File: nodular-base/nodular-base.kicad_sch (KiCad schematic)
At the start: 0 parts

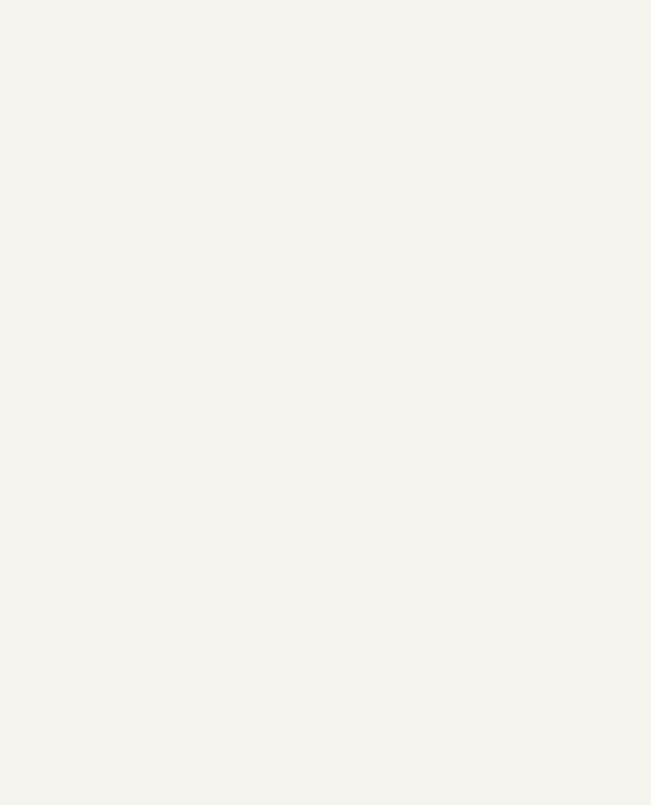
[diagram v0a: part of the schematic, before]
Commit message: Update layout for top board, add library items
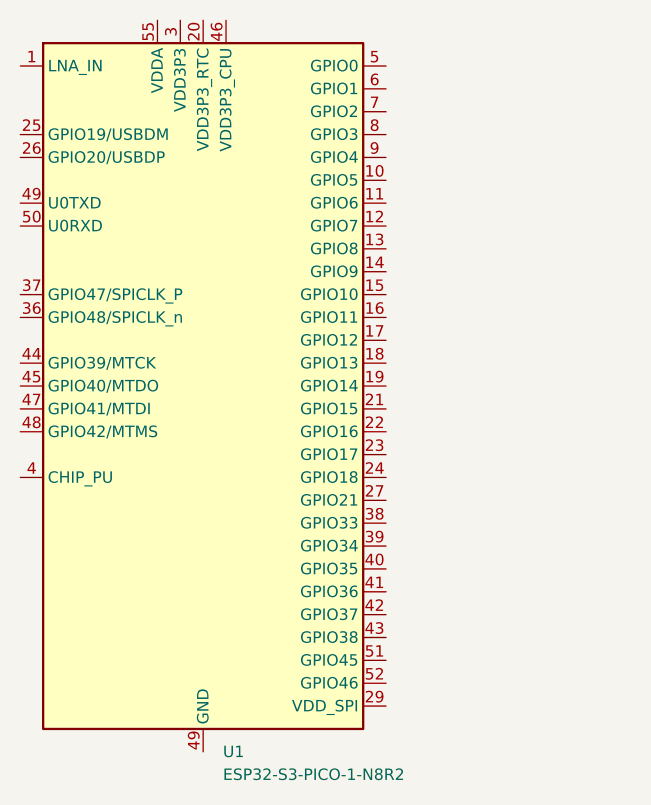
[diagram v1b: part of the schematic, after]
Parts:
- added U1: ESP32-S3-PICO-1-N8R2, Package_DFN_QFN:QFN-56-1EP_7x7mm_P0.4mm_EP4x4mm, symbol nodular:ESP32-S3-PICO-1-N8R2
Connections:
- new net: U1.2 (VDD3P3), U1.3 (VDD3P3)
- new net: U1.55 (VDDA), U1.56 (VDDA)
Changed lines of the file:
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@@
 (kicad_sch (version 20230121) (generator eeschema)
   (paper "A4")
+  (symbol (lib_id "nodular:ESP32-S3-PICO-1-N8R2") (at 90.17 100.33 0) (unit 1)
+    (in_bom yes) (on_board yes) (dnp no) (fields_autoplaced)
+    (property "Reference" "U1" (at 92.3641 140.97 0)
+      (effects (font (size 1.27 1.27)) (justify left))
+    )
+    (property "Value" "ESP32-S3-PICO-1-N8R2" (at 92.3641 143.51 0)
+      (effects (font (size 1.27 1.27)) (justify left))
+    )
+    (property "Footprint" "Package_DFN_QFN:QFN-56-1EP_7x7mm_P0.4mm_EP4x4mm" (at 90.17 143.51 0)
+      (effects (font (size 1.27 1.27)) hide)
+    )
+    (property "Datasheet" "" (at 90.17 145.796 0)
+      (effects (font (size 1.27 1.27)) hide)
+    )
+    (pin "36")
+    (pin "51")
+    (pin "44")
+    (pin "24")
+    (pin "21")
+    (pin "43")
+    (pin "35")
+    (pin "7")
+    (pin "22")
+    (pin "23")
+    (pin "16")
+    (pin "42")
+    (pin "9")
+    (pin "33")
+    (pin "2")
+    (pin "48")
+    (pin "50")
+    (pin "26")
+    (pin "34")
+    (pin "41")
+    (pin "37")
+    (pin "8")
+    (pin "46")
+    (pin "19")
+    (pin "49")
+    (pin "12")
+    (pin "13")
+    (pin "38")
+    (pin "52")
+    (pin "1")
+    (pin "11")
+    (pin "31")
+    (pin "14")
+    (pin "47")
+    (pin "15")
+    (pin "30")
+    (pin "18")
+    (pin "5")
+    (pin "10")
+    (pin "55")
+    (pin "45")
+    (pin "27")
+    (pin "56")
+    (pin "25")
+    (pin "32")
+    (pin "39")
+    (pin "6")
+    (pin "28")
+    (pin "29")
+    (pin "4")
+    (pin "3")
+    (pin "49")
+    (pin "17")
+    (pin "40")
+    (pin "20")
+    (instances
+      (project "nodular-base"
+        (path "/6dcb0502-87e2-4c28-9ce8-81aab8925f06"
+          (reference "U1") (unit 1)
+        )
+      )
+    )
+  )
   (sheet (at 180.34 64.77) (size 46.99 46.99) (fields_autoplaced)
     (stroke (width 0.1524) (type solid))

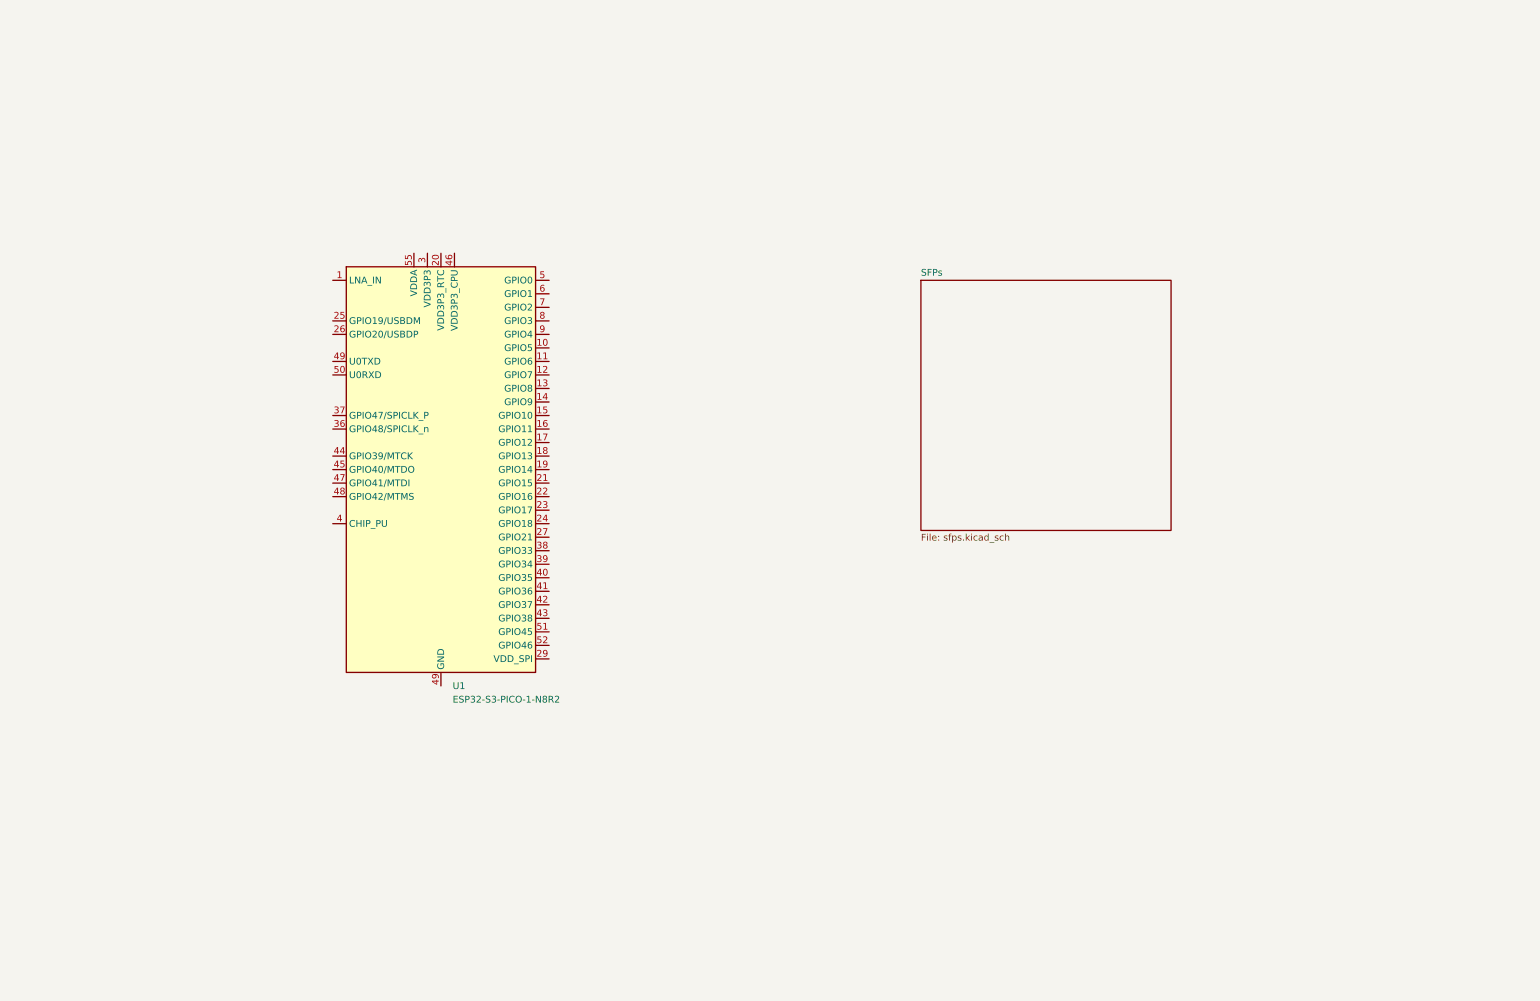
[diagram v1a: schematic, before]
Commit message: Nodular-base: Add most components onto baseboard for a test fit. Nodular-base: Add fps and models for solderable standoffs, replace solderable standoffs and reposition them. Nodule template: Adjust nodule template hole position, export STEP of nodule. Nodular-base: Add many components to schematic, structure schematic hierarchy Nodular-base: Route USB, RF path, and MCU decoupling
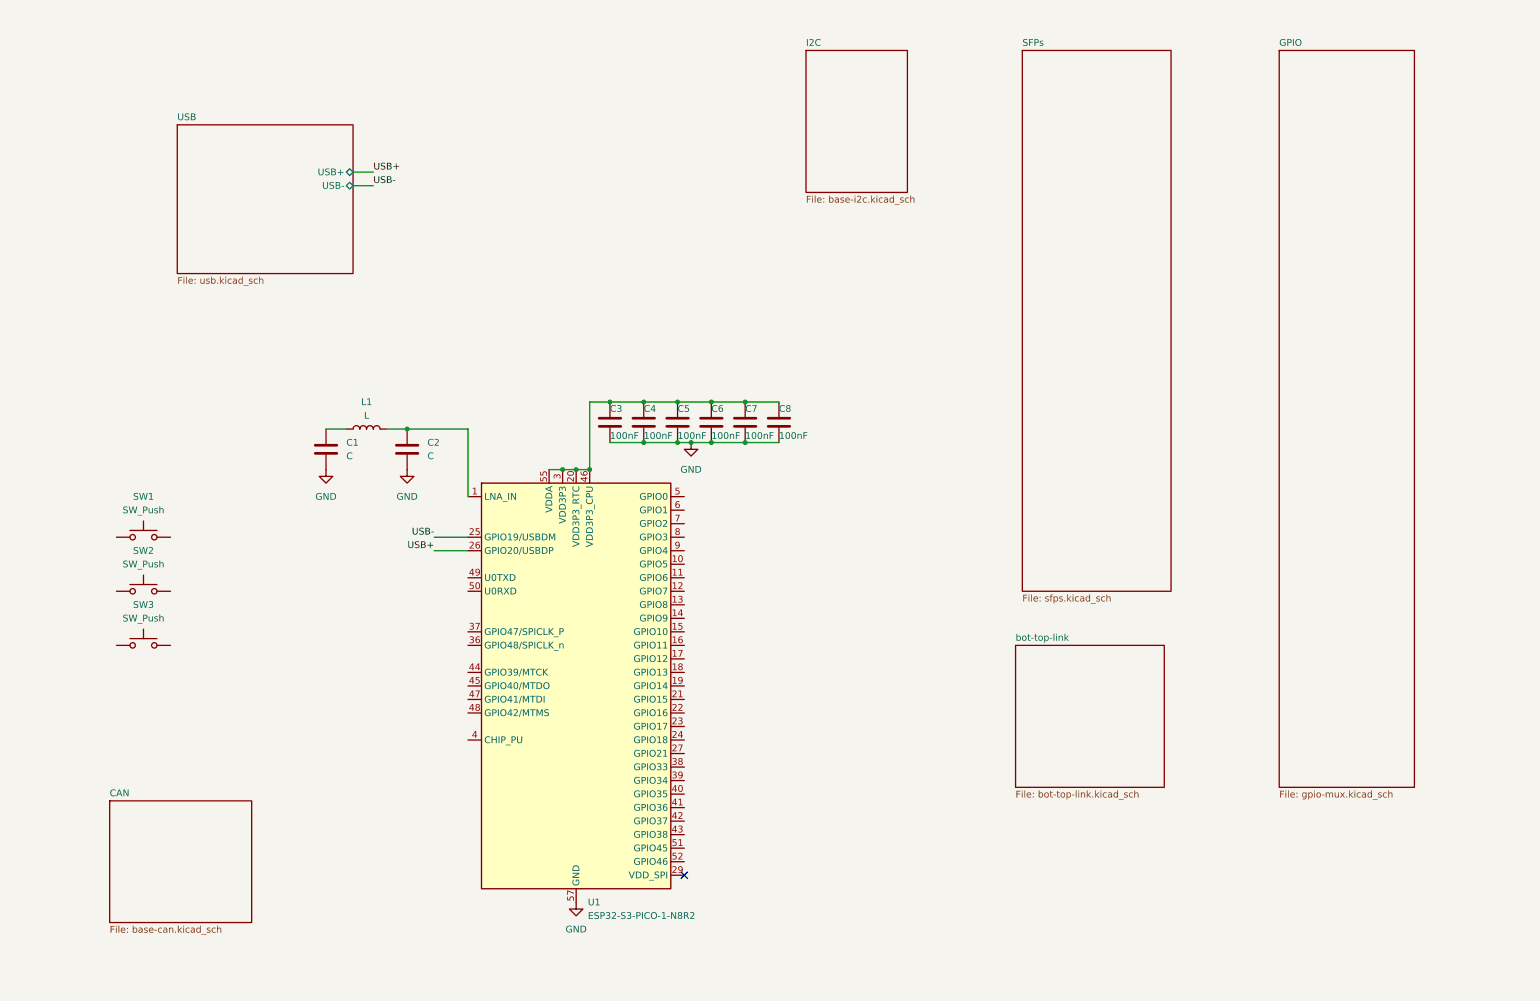
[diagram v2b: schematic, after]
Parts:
- added C1, C2: C, Capacitor_SMD:C_0402_1005Metric, symbol Device:C
- added C3, C4, C5, C6, C7, C8: 100nF, Capacitor_SMD:C_0402_1005Metric, symbol Device:C
- added L1: L, Inductor_SMD:L_0402_1005Metric, symbol Device:L
- added SW1, SW2, SW3: SW_Push, nodular:sidebutton-1TS003B-1400-3500A-CT, symbol Switch:SW_Push
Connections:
- net at U1.1 (LNA_IN): now also C2.1, L1.2
- net at U1.2 (VDD3P3), U1.3 (VDD3P3): now also U1.20 (VDD3P3_RTC), U1.46 (VDD3P3_CPU), U1.55 (VDDA), U1.56 (VDDA), C3.1, C4.1, C5.1, C6.1, C7.1, C8.1
- net USB-: now reaches U1.25 (GPIO19/USBDM)
- net USB+: now reaches U1.26 (GPIO20/USBDP)
- new net: C1.1, L1.1
- new net GND: C1.2, C2.2, C3.2, C4.2, C5.2, C6.2, C7.2, C8.2, U1.57 (GND)
- no-connect marks 0 -> 1
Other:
- added sheet CAN (base-can.kicad_sch)
- added sheet GPIO (gpio-mux.kicad_sch)
- added sheet I2C (base-i2c.kicad_sch)
- added sheet USB (usb.kicad_sch)
- added sheet bot-top-link (bot-top-link.kicad_sch)
- moved on the sheet: U1

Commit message: WIP layout for base
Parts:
- added C9: 22uF, Capacitor_SMD:C_1206_3216Metric, symbol Device:C
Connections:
- net GND: now also C9.2
- net 3V3_SYS: now reaches C3.1, C4.1, C5.1, C6.1, C7.1, C8.1, U1.2 (VDD3P3), U1.20 (VDD3P3_RTC), U1.3 (VDD3P3), U1.46 (VDD3P3_CPU), U1.55 (VDDA), U1.56 (VDDA)
- net 3V3_SYS: now also C9.1
- net NF_HS3: now reaches U1.10 (GPIO5)
- net NF_HS4: now reaches U1.11 (GPIO6)
- net ND_HS1: now reaches U1.16 (GPIO11)
- net ND_HS4: now reaches U1.17 (GPIO12)
- net ND_HS3: now reaches U1.18 (GPIO13)
- net ND_HS2: now reaches U1.19 (GPIO14)
- net NE_HS3: now reaches U1.21 (GPIO15)
- net NE_HS2: now reaches U1.22 (GPIO16)
- net NE_HS4: now reaches U1.23 (GPIO17)
- net NE_HS1: now reaches U1.24 (GPIO18)
- net LED_DATA: now reaches U1.27 (GPIO21)
- net NC_HS4: now reaches U1.36 (GPIO48/SPICLK_n)
- net NC_HS3: now reaches U1.37 (GPIO47/SPICLK_P)
- net NC_HS2: now reaches U1.38 (GPIO33)
- net NC_HS1: now reaches U1.39 (GPIO34)
- net NB_HS1: now reaches U1.40 (GPIO35)
- net NB_HS2: now reaches U1.41 (GPIO36)
- net NB_HS3: now reaches U1.42 (GPIO37)
- net NB_HS4: now reaches U1.43 (GPIO38)
- net NA_HS1: now reaches U1.44 (GPIO39/MTCK)
- net NA_HS2: now reaches U1.45 (GPIO40/MTDO)
- net NA_HS3: now reaches U1.47 (GPIO41/MTDI)
- net NA_HS4: now reaches U1.48 (GPIO42/MTMS)
- net NF_HS1: now reaches U1.8 (GPIO3)
- net NF_HS2: now reaches U1.9 (GPIO4)
- no-connect marks 1 -> 2
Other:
- sheet GPIO ports: added 3V3_SYS, ALS1, ALS2, ALS3, ALS4, ALS5, BLS1, BLS2, BLS3, BLS4, BLS5, BTN1, BTN2, BTN3, BTN4, BTN5, BTN6, CAN_EN, CLS1, CLS2, CLS3, CLS4, CLS5, DET_A, DET_B, DET_C, DET_D, DET_E, DET_F, DLS1, DLS2, DLS3, DLS4, DLS5, ELS1, ELS2, ELS3, ELS4, ELS5, FLS1, FLS2, FLS3, FLS4, FLS5, LED_PWR_EN, SCL_SYS, SDA_SYS, ~{INT_SYS}; removed none
- sheet I2C ports: added SCL_A, SCL_B, SCL_C, SCL_D, SCL_E, SCL_F, SCL_SYS, SDA_A, SDA_B, SDA_C, SDA_D, SDA_E, SDA_F, SDA_SYS; removed none
- sheet SFPs ports: added AH1, AH2, AH3, AH4, ALS1, ALS2, ALS3, ALS4, ALS5, BH1, BH2, BH3, BH4, BLS1, BLS2, BLS3, BLS4, BLS5, CH1, CH2, CH3, CH4, CLS1, CLS2, CLS3, CLS4, CLS5, DH1, DH2, DH3, DH4, DLS1, DLS2, DLS3, DLS4, DLS5, EH1, EH2, EH3, EH4, ELS1, ELS2, ELS3, ELS4, ELS5, FH1, FH2, FH3, FH4, FLS1, FLS2, FLS3, FLS4, FLS5, ND_PS_A, ND_PS_B, ND_PS_C, ND_PS_D, ND_PS_E, ND_PS_F, SCL_A, SCL_B, SCL_C, SCL_D, SCL_E, SCL_F, SDA_A, SDA_B, SDA_C, SDA_D, SDA_E, SDA_F; removed none
- sheet USB ports: added 3V3_SYS, BAT+, SCL, SDA, VSYS, ~{QON}; removed none
- sheet bot-top-link ports: added LED_DATA, LED_EN; removed none
- moved on the sheet: C1, C2, C3, C4, C5, C6, C7, C8, L1, SW1, SW2, SW3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

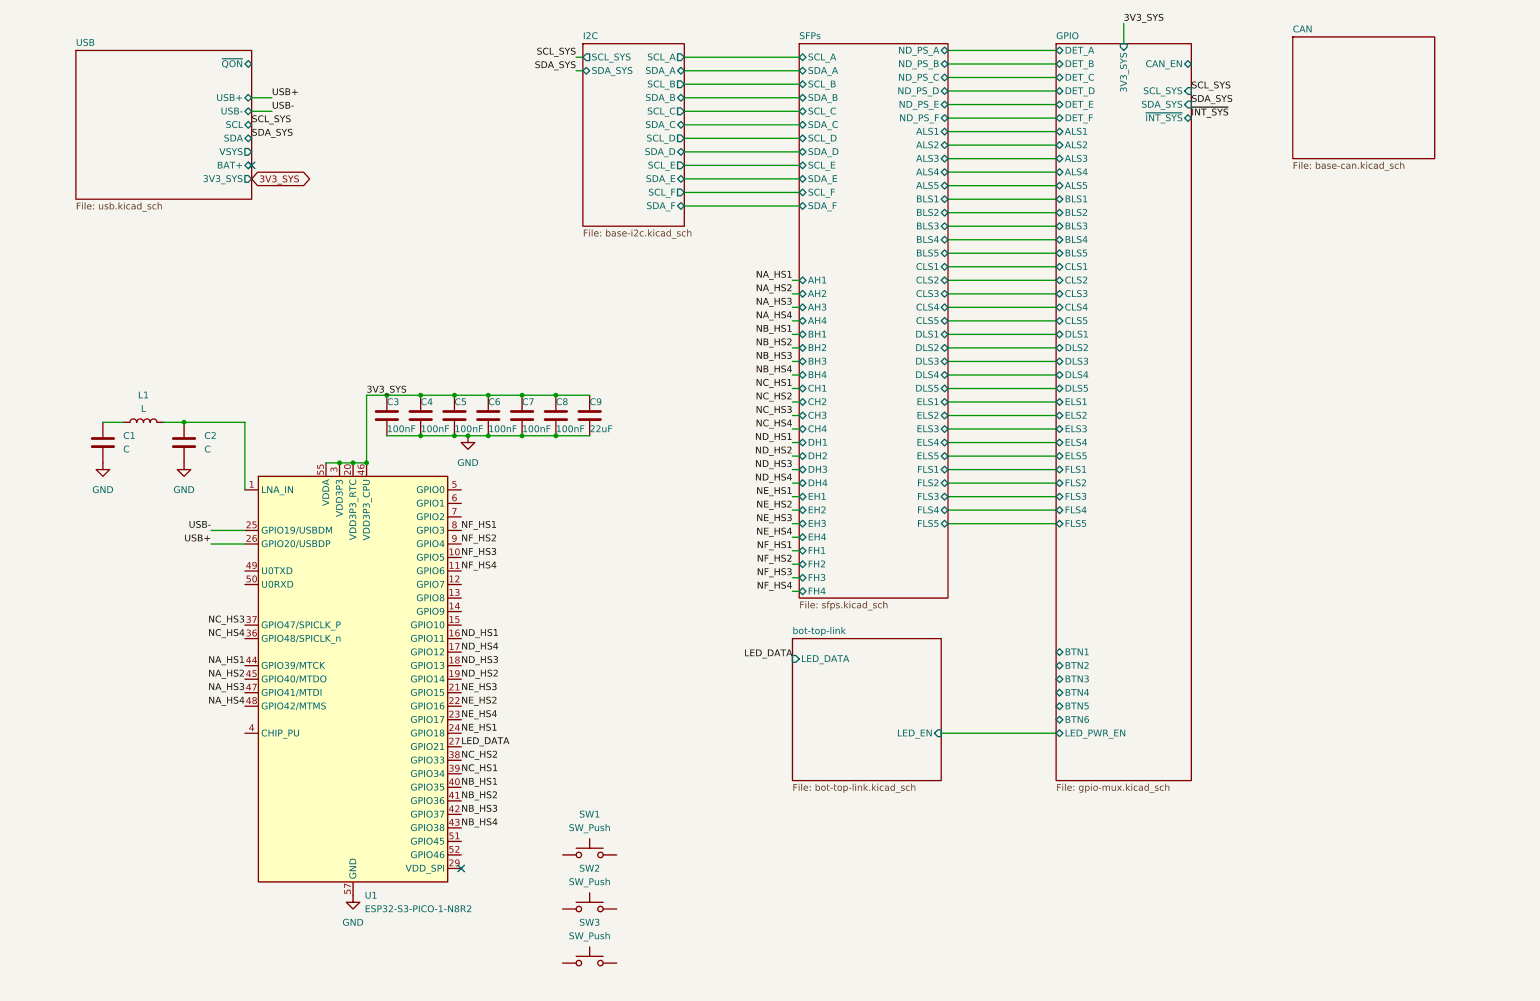
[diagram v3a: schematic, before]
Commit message: Switched from CAN to USB for second USB-C port Added second PD controller and USB mux to allow switching between host and device port Added SOICbite to corner All routing complete Updated pin map, added i2c addresses, soicbit pin mapping, and fpc pinout to document
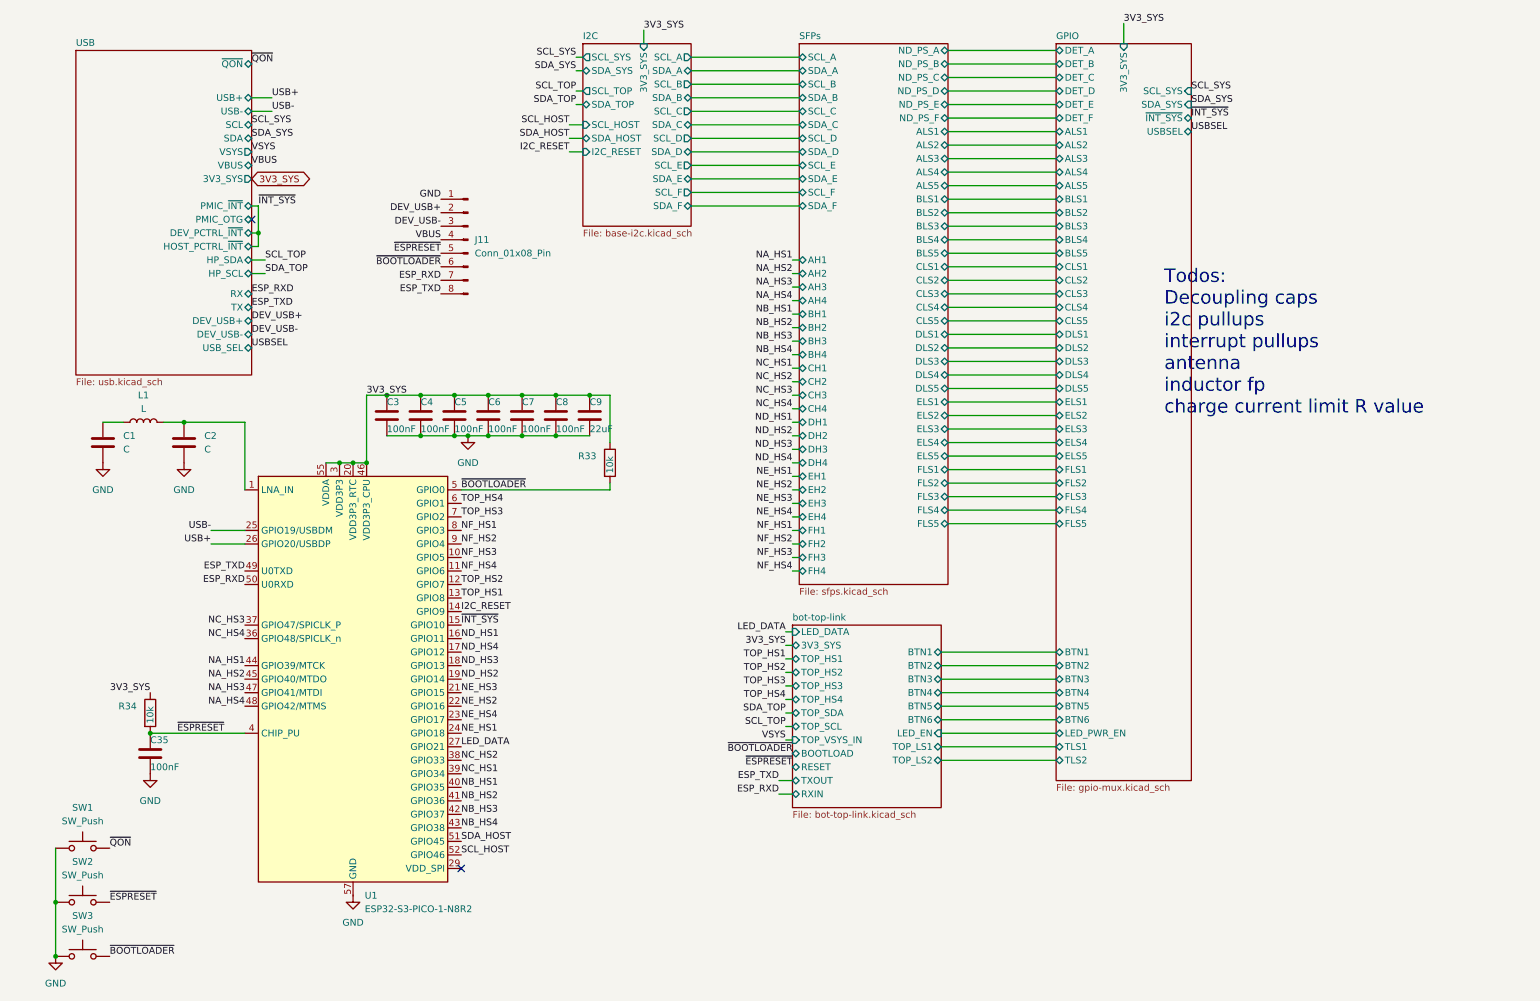
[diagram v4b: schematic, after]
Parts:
- added C35: 100nF, Capacitor_SMD:C_0402_1005Metric, symbol Device:C
- added J11: Conn_01x08_Pin, nodular:SOIC_clipProgSmall, symbol Connector:Conn_01x08_Pin
- added R33, R34: 10k, Resistor_SMD:R_0402_1005Metric, symbol Device:R
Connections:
- net 3V3_SYS: now also R33.1, R34.1
- net GND: now also SW1.1, SW2.1, SW3.1, C35.2, J11.1 (Pin_1)
- net ~{INT_SYS}: now also U1.15 (GPIO10)
- net ~{QON}: now reaches SW1.2
- net ~{BOOTLOADER}: now reaches SW3.2
- net ~{BOOTLOADER}: now also U1.5 (GPIO0), J11.6 (Pin_6), R33.2
- net TOP_HS2: now reaches U1.12 (GPIO7)
- net TOP_HS1: now reaches U1.13 (GPIO8)
- net I2C_RESET: now reaches U1.14 (GPIO9)
- net ~{ESPRESET}: now reaches U1.4 (CHIP_PU)
- net ~{ESPRESET}: now also SW2.2, C35.1, J11.5 (Pin_5), R34.2
- net ESP_TXD: now reaches U1.49 (U0TXD)
- net ESP_TXD: now also J11.8 (Pin_8)
- net ESP_RXD: now reaches U1.50 (U0RXD)
- net ESP_RXD: now also J11.7 (Pin_7)
- net SDA_HOST: now reaches U1.51 (GPIO45)
- net SCL_HOST: now reaches U1.52 (GPIO46)
- net TOP_HS4: now reaches U1.6 (GPIO1)
- net TOP_HS3: now reaches U1.7 (GPIO2)
- new net DEV_USB+: J11.2 (Pin_2)
- new net DEV_USB-: J11.3 (Pin_3)
- new net VBUS: J11.4 (Pin_4)
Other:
- removed sheet CAN
- sheet GPIO ports: added TLS1, TLS2, USBSEL; removed CAN_EN
- sheet I2C ports: added 3V3_SYS, I2C_RESET, SCL_HOST, SCL_TOP, SDA_HOST, SDA_TOP; removed none
- sheet USB ports: added DEV_PCTRL_~{INT}, DEV_USB+, DEV_USB-, HOST_PCTRL_~{INT}, HP_SCL, HP_SDA, PMIC_OTG, PMIC_~{INT}, RX, TX, USB_SEL, VBUS; removed BAT+
- sheet bot-top-link ports: added 3V3_SYS, BOOTLOAD, BTN1, BTN2, BTN3, BTN4, BTN5, BTN6, RESET, RXIN, TOP_HS1, TOP_HS2, TOP_HS3, TOP_HS4, TOP_LS1, TOP_LS2, TOP_SCL, TOP_SDA, TOP_VSYS_IN, TXOUT; removed none
- note added: "Todos: Decoupling caps i2c pullups interrupt pullups antenna inductor fp charge current limit R value"
- moved on the sheet: SW1, SW2, SW3
